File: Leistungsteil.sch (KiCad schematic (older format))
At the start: 45 parts, among them J18 Conn_01x02_Male, J19 Conn_01x02_Male, J20 Conn_01x02_Male, J21 OSTTC022162, J22 Conn_01x02_Male, J23 Conn_01x02_Male, J24 Conn_01x02_Male, Q10 TIP3055, Q11 TIP3055, Q12 TIP3055, Q6 BS170, Q7 TIP3055, Q8 TIP3055, Q9 TIP3055, U7 TL072

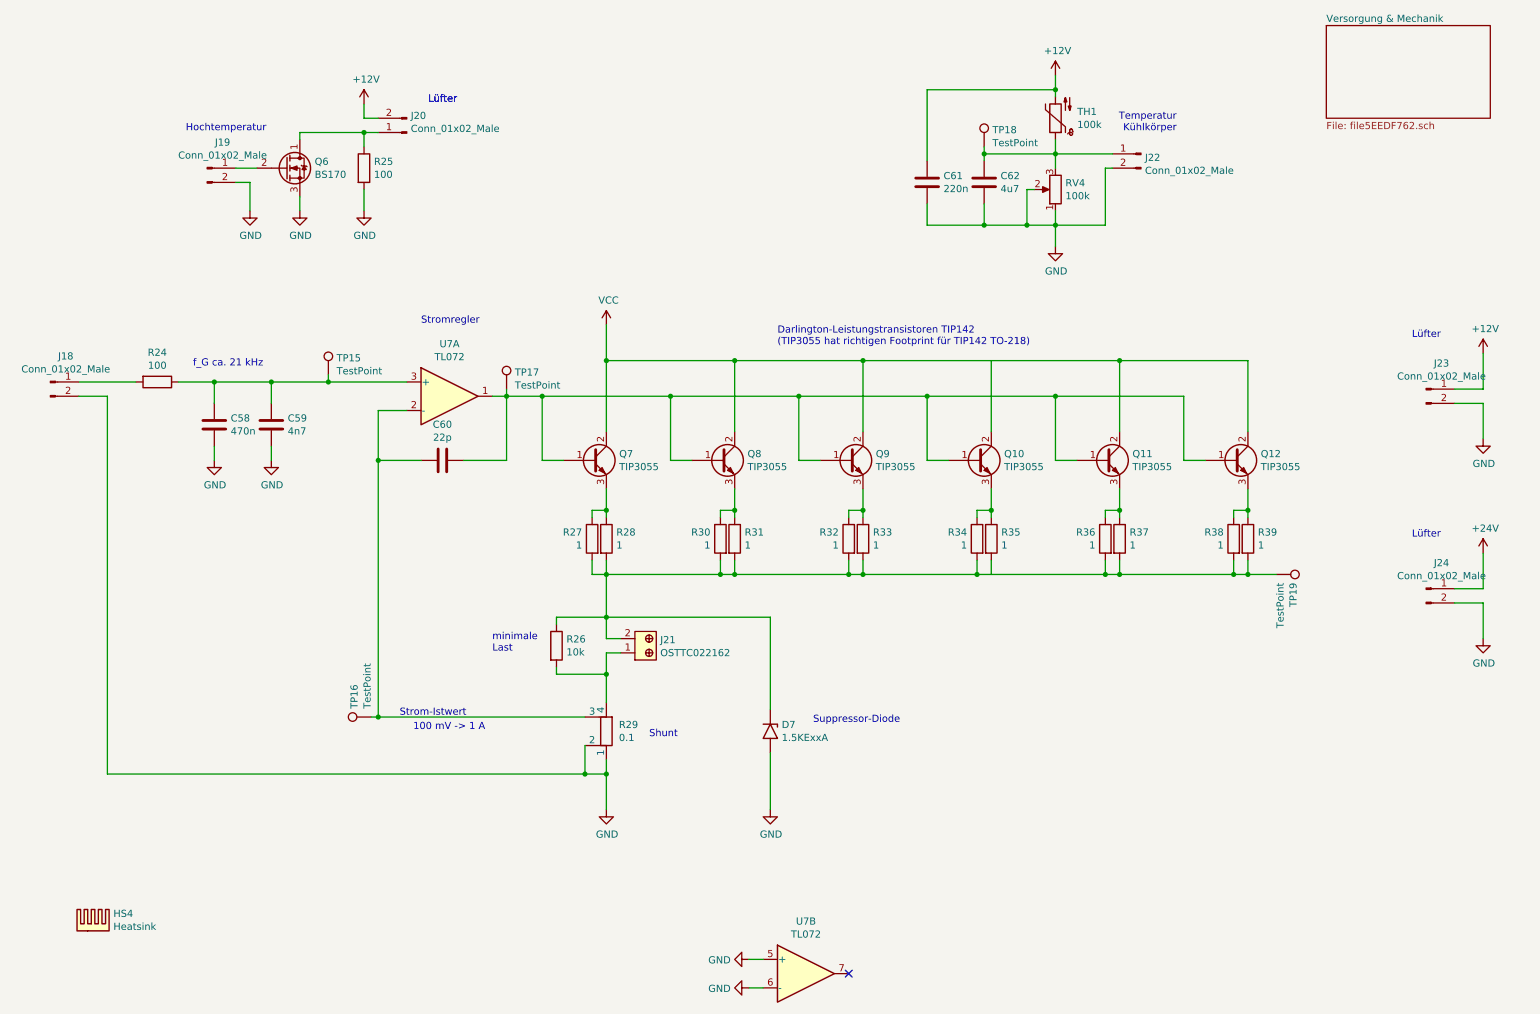
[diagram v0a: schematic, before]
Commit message: change to SMD 1206 and restructuring
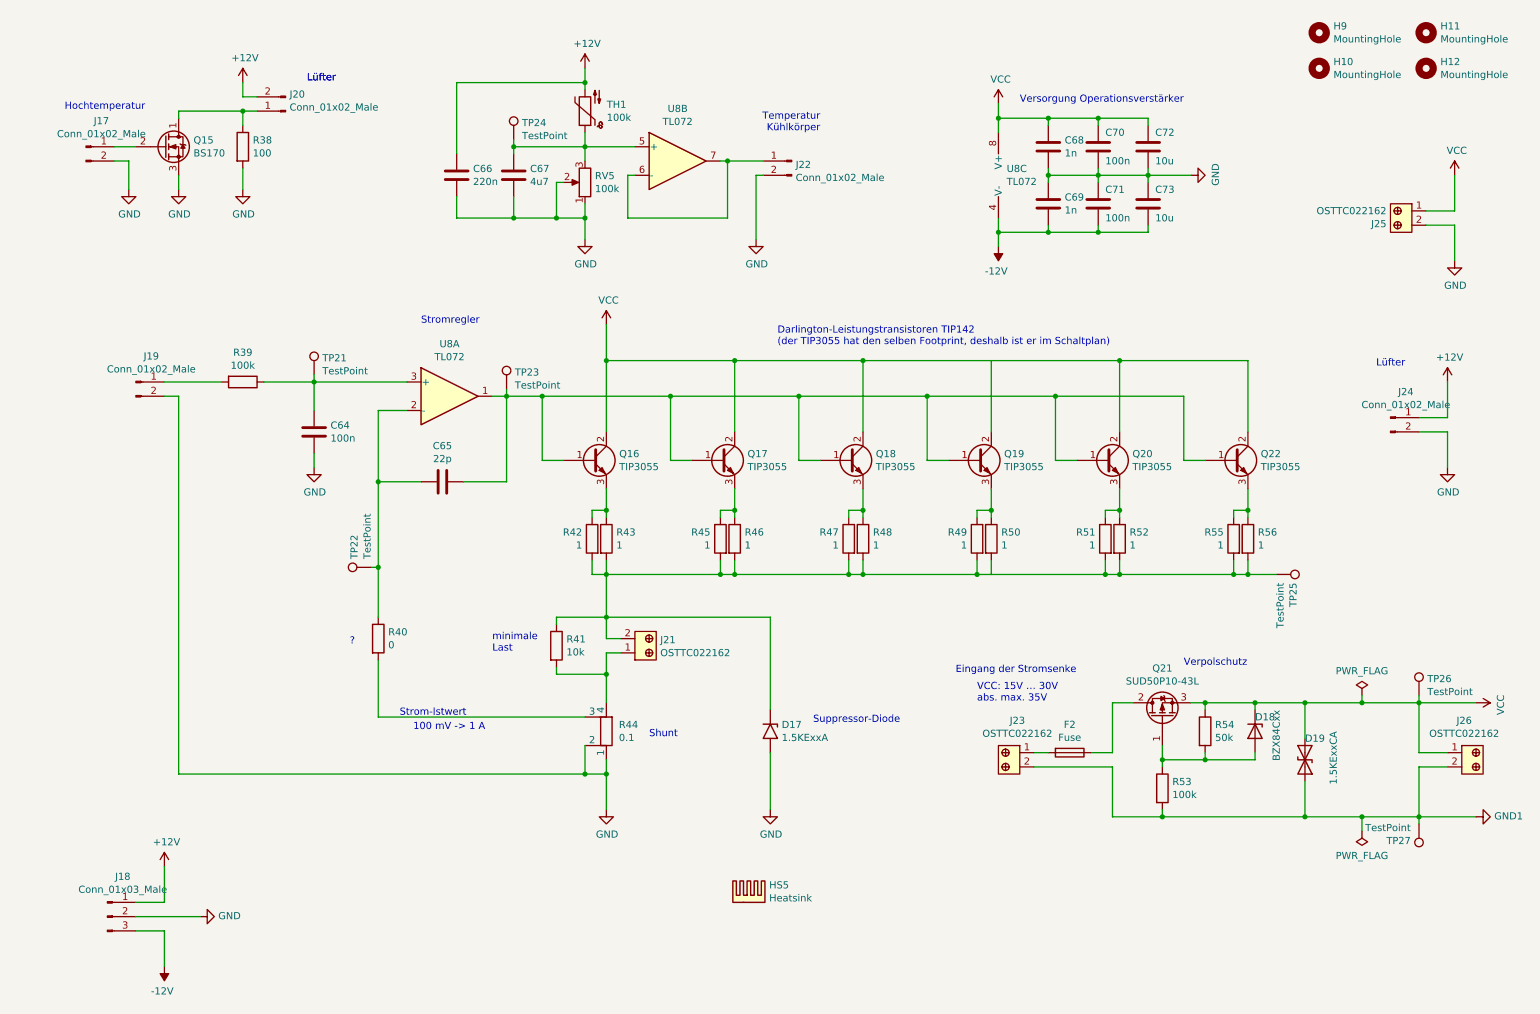
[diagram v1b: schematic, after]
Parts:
- removed C59: 4n7, symbol Device:C
- removed J24: Conn_01x02_Male, symbol Connector:Conn_01x02_Male
- removed Q10, Q11, Q12, Q7, Q8, Q9: TIP3055, Package_TO_SOT_THT:TO-218-3_Vertical, symbol Transistor_BJT:TIP3055
- removed U7: TL072, symbol Amplifier_Operational:TL072
- added C68, C69: 1n, Capacitor_SMD:C_0805_2012Metric_Pad1.15x1.40mm_HandSolder, symbol Device:C
- added C70, C71: 100n, Capacitor_SMD:C_0805_2012Metric_Pad1.15x1.40mm_HandSolder, symbol Device:C
- added C72, C73: 10u, Capacitor_SMD:C_0805_2012Metric_Pad1.15x1.40mm_HandSolder, symbol Device:C
- added D18: BZX84Cxx, Diode_SMD:D_SOT-23_ANK, symbol Diode:BZX84Cxx
- added D19: 1.5KExxCA, Diode_THT:D_DO-201AE_P15.24mm_Horizontal, symbol Diode:1.5KExxCA
- added F2: Fuse, Fuse:Fuseholder_Cylinder-5x20mm_EATON_HBW_Vertical_Closed, symbol Device:Fuse
- added H10, H11, H12, H9: MountingHole, MountingHole:MountingHole_3.2mm_M3_DIN965, symbol Mechanical:MountingHole
- added J18: Conn_01x03_Male, symbol Connector:Conn_01x03_Male
- added J23, J25, J26: OSTTC022162, digikey-footprints:Term_Block_1x2_P5.08MM, symbol dk_Terminal-Blocks-Wire-to-Board:OSTTC022162
- added Q16, Q17, Q18, Q19, Q20, Q22: TIP3055, Package_TO_SOT_THT:TO-218-3_Vertical, symbol Transistor_BJT:TIP3055
- added Q21: SUD50P10-43L, Package_TO_SOT_SMD:TO-252-2, symbol Transistor_FET:SUD50P10-43L
- added R40: 0, symbol Device:R
- added R53: 100k, Resistor_SMD:R_0805_2012Metric_Pad1.15x1.40mm_HandSolder, symbol Device:R
- added R54: 50k, Resistor_SMD:R_0805_2012Metric_Pad1.15x1.40mm_HandSolder, symbol Device:R
- added TP26, TP27: TestPoint, symbol Connector:TestPoint
- added U8: TL072, Package_DIP:DIP-8_W7.62mm_Socket, symbol Amplifier_Operational:TL072
- C64: renamed from C58; value 470n -> 100n
- R39: renamed from R24; value 100 -> 100k
- renumbered C60 to C65, C61 to C66, C62 to C67, D7 to D17, HS4 to HS5, J19 to J17, J18 to J19, J23 to J24, Q6 to Q15, R25 to R38, R26 to R41, R27 to R42, R28 to R43, R29 to R44, R30 to R45, R31 to R46, R32 to R47, R33 to R48, R34 to R49, R35 to R50, R36 to R51, R37 to R52, R38 to R55, R39 to R56, RV4 to RV5, TP15 to TP21, TP16 to TP22, TP17 to TP23, TP18 to TP24, TP19 to TP25
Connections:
- net +12V: now also J18.1 (Pin_1)
- net GND: now also C68.2, C69.1, C70.2, C71.1, C72.2, C73.1, J18.2 (Pin_2), J25.2
- net VCC: now also C68.1, C70.1, C72.1, D18.1 (K), D19.1 (A1), J25.1, J26.1, Q16.2 (C), Q17.2 (C), Q18.2 (C), Q19.2 (C), Q20.2 (C), Q21.3 (S), Q22.2 (C), R54.1, TP26.1, U8.8 (V+)
- net at C65.1, TP23.1: now also Q16.1 (B), Q17.1 (B), Q18.1 (B), Q19.1 (B), Q20.1 (B), Q22.1 (B), U8.1
- net at C64.1, R39.1, TP21.1: now also U8.3 (+)
- net at C67.1, RV5.3, TH1.1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: now also U8.5 (+); no longer J22.1 (Pin_1)
- net at R42.1, R43.1: now also Q16.3 (E)
- net at R55.1, R56.1: now also Q22.3 (E)
- net at R49.1, R50.1: now also Q19.3 (E)
- net at R47.1, R48.1: now also Q18.3 (E)
- net at R45.1, R46.1: now also Q17.3 (E)
- net at C65.2, TP22.1: now also R40.1, U8.2 (-); no longer R44.3
- net at R51.1, R52.1: now also Q20.3 (E)
- new net: J22.1 (Pin_1), U8.6 (-), U8.7
- new net: R40.2, R44.3
- new net: F2.1, Q21.2 (D)
- new net: F2.2, J23.1
- new net: D18.2 (A), Q21.1 (G), R53.1, R54.2
- new net -12V: C69.2, C71.2, C73.2, J18.3 (Pin_3), U8.4 (V-)
- new net GND1: D19.2 (A2), J23.2, J26.2, R53.2, TP27.1
- no-connect marks 1 -> 0
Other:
- note added: "?"
- note added: "Darlington-Leistungstransistoren TIP142\n(der TIP3055 hat den selben Footprint, deshalb ist er im Schaltplan)"
- note added: "Eingang der Stromsenke"
- note added: "VCC: 15V … 30V\nabs. max. 35V"
- note added: "Verpolschutz"
- note added: "Versorgung Operationsverstärker"
- note removed: "Darlington-Leistungstransistoren TIP142\n(TIP3055 hat richtigen Footprint für TIP142 TO-218)"
- note removed: "f_G ca. 21 kHz"
- moved on the sheet: C64, C65, C66, C67, HS5, J17, J19, J20, J22, J24, Q15, R38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
